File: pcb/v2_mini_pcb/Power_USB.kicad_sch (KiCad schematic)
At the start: 39 parts, among them J6 USB4105-GF-A, U10 TPS63802DLAR, U6 TPD4EUSB30, U8 BQ25622ERYKR, U9 MAX17048G_T10

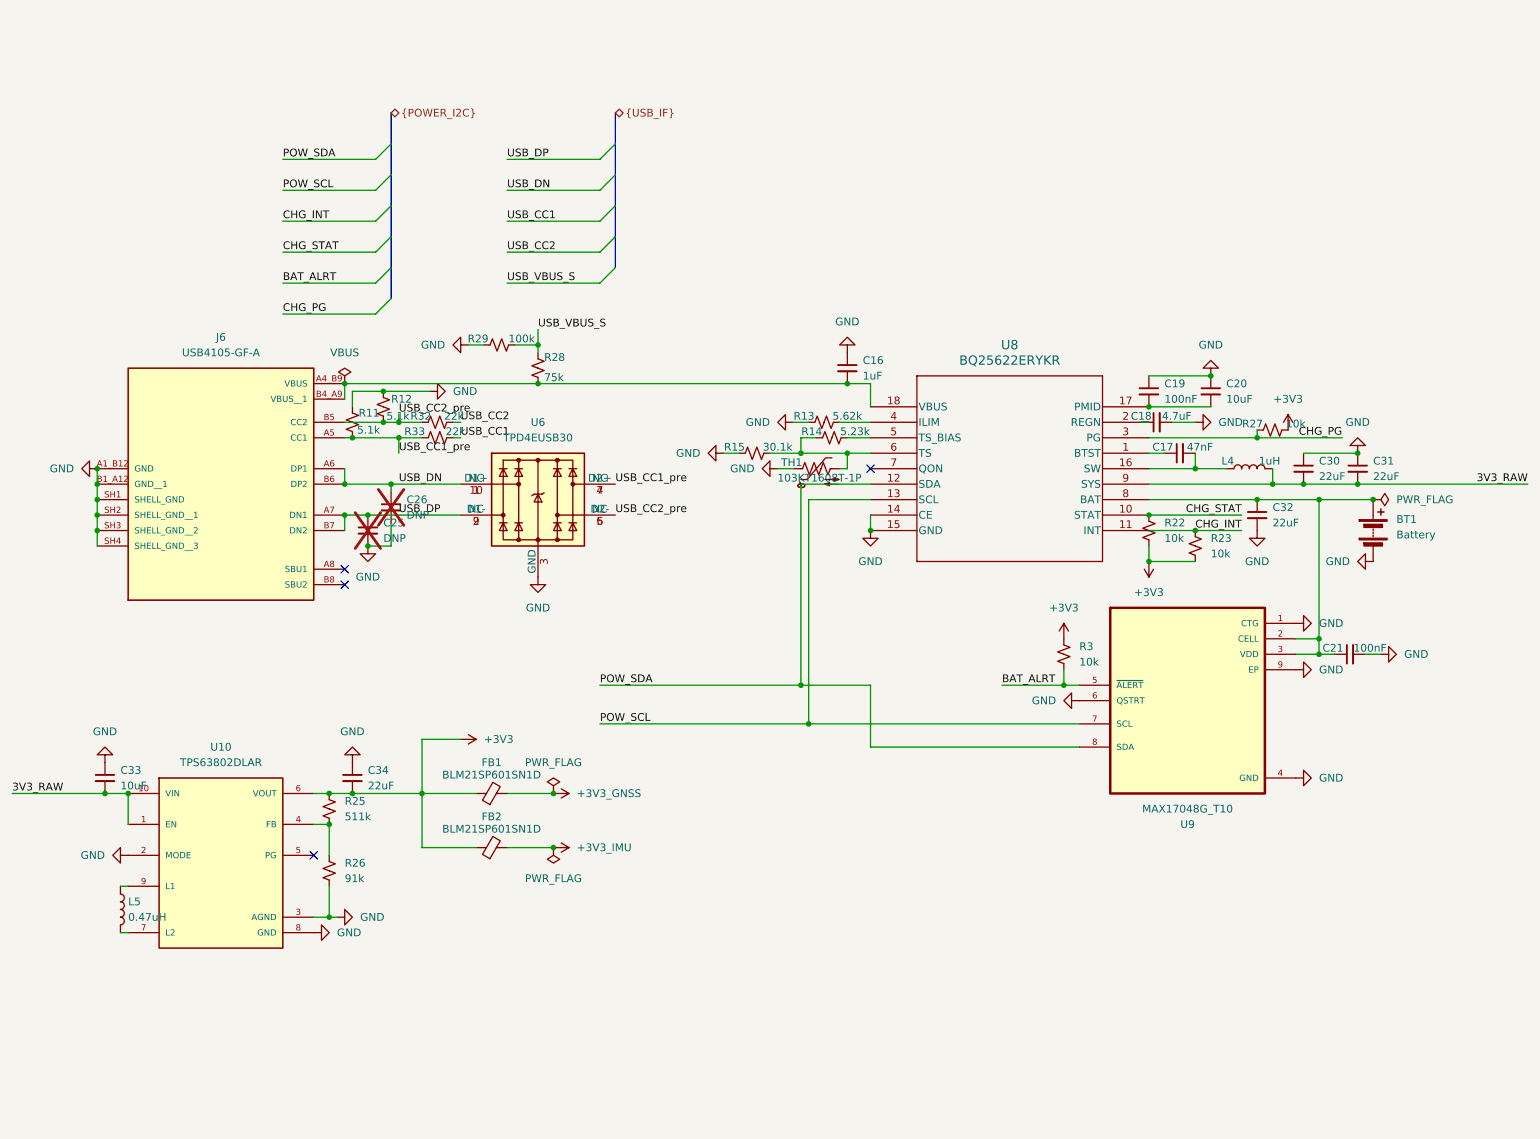
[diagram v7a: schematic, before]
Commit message: add power off schematic
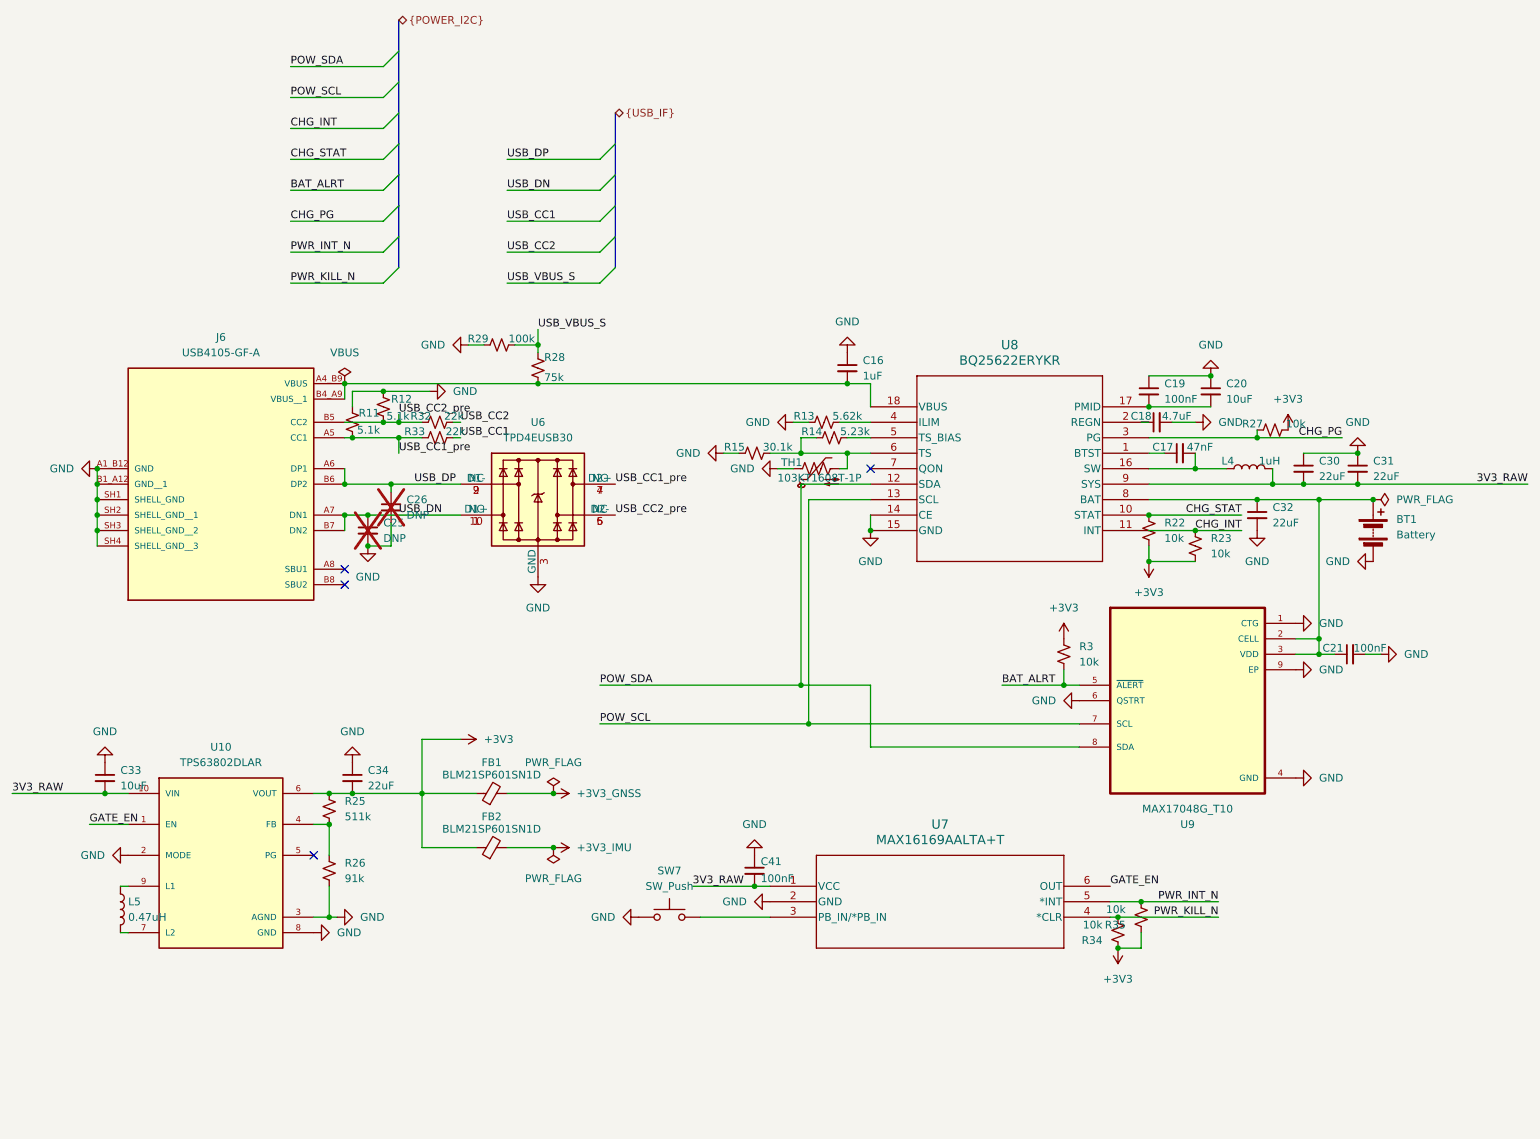
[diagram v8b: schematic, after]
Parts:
- added C41: 100nF, Capacitor_SMD:C_0402_1005Metric, symbol Device:C_Small
- added R34, R35: 10k, Resistor_SMD:R_0402_1005Metric, symbol Device:R_Small_US
- added SW7: SW_Push, Button_Switch_SMD:SW_SPST_B3U-1000P, symbol Switch:SW_Push
- added U7: MAX16169AALTA+T, all:21-0164_L622&plus_1_ADI, symbol all:MAX16169AALTA+T
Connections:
- net +3V3: now also R34.1, R35.1
- net 3V3_RAW: now also C41.2, U7.1 (VCC); no longer U10.1 (EN)
- net GND: now also C41.1, SW7.1, U7.2 (GND)
- net USB_DN: now also C25.1, J6.A7 (DN1), J6.B7 (DN2); no longer C26.1, J6.A6 (DP1), J6.B6 (DP2)
- net USB_DP: now also C26.1, J6.A6 (DP1), J6.B6 (DP2); no longer C25.1, J6.A7 (DN1), J6.B7 (DN2)
- new net: SW7.2, U7.3 (PB_IN/*PB_IN)
- new net GATE_EN: U10.1 (EN), U7.6 (OUT)
- new net PWR_INT_N: R35.2, U7.5 (*INT)
- new net PWR_KILL_N: R34.2, U7.4 (*CLR)
